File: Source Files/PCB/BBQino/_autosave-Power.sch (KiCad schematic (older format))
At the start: 14 parts, among them J1 VIN < 13V, Q1 IPD068P03L3G, U1 ADP7142ARDZ-5.0

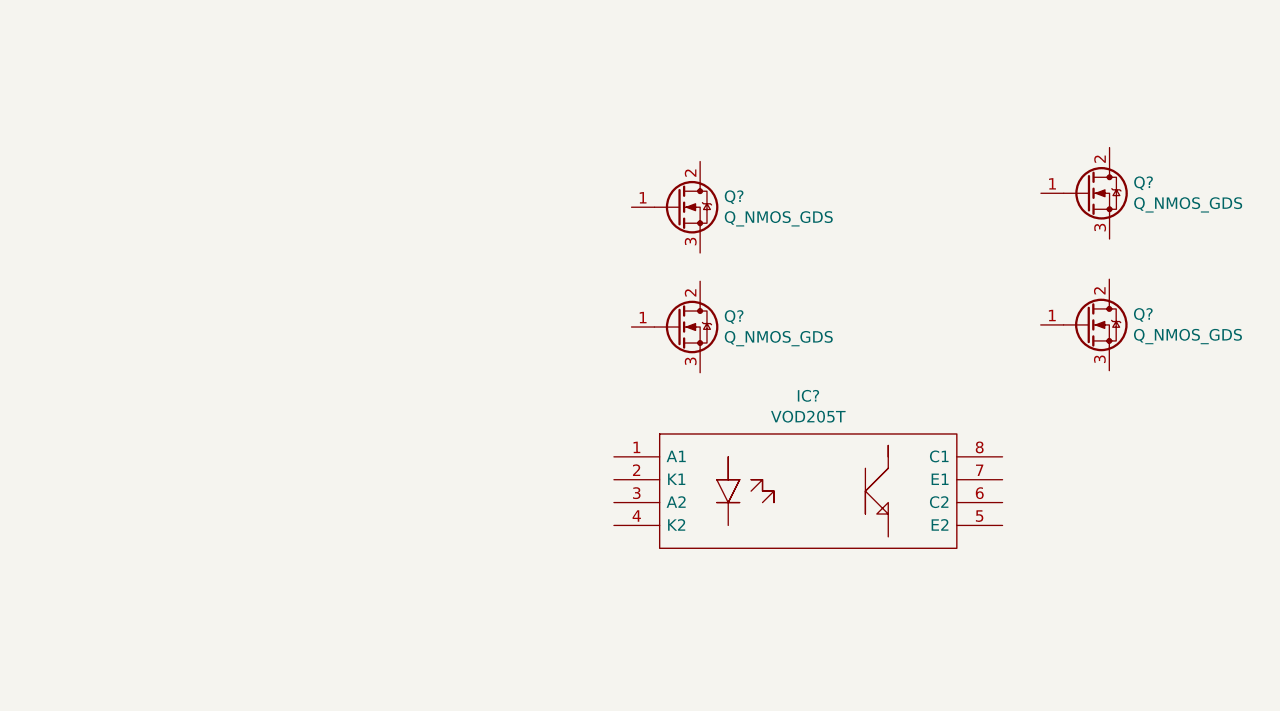
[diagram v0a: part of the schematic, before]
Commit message: added thermocouple interface
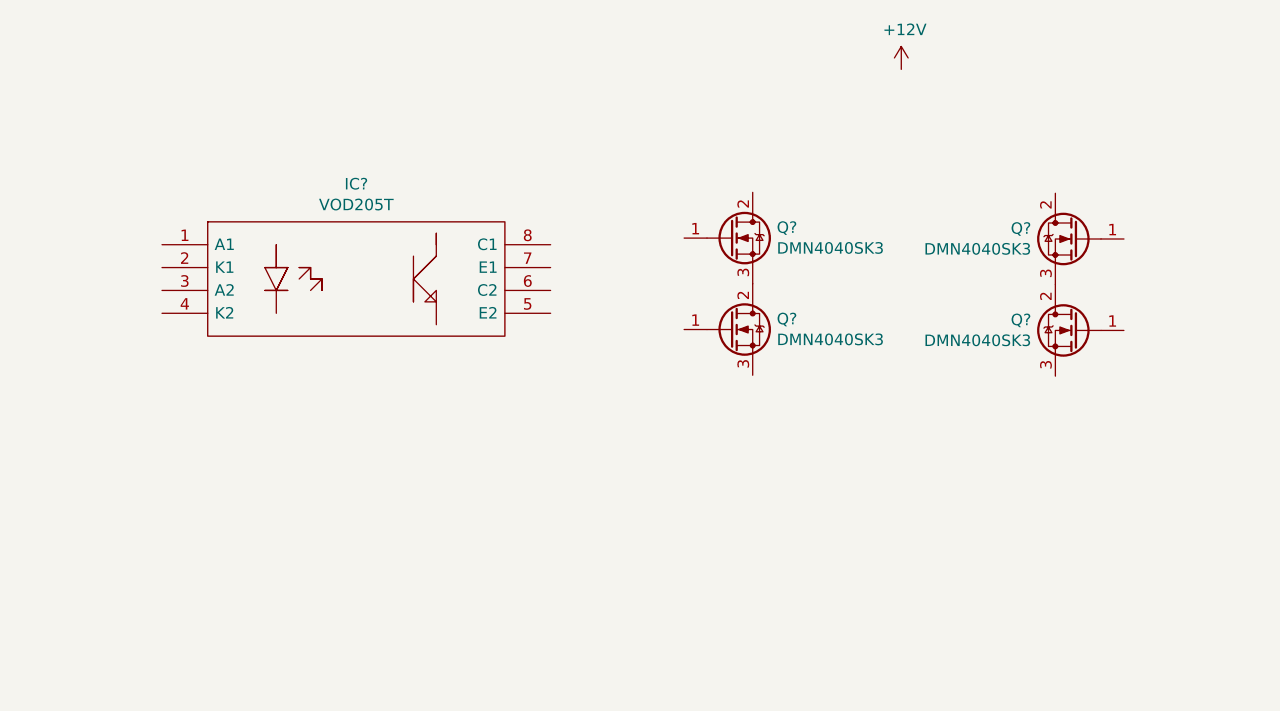
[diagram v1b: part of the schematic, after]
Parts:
- removed Q? (x3): Q_NMOS_GDS, symbol Device:Q_NMOS_GDS
- added Q? (x3): DMN4040SK3, Package_TO_SOT_SMD:TO-252-3_TabPin2, symbol Device:Q_NMOS_GDS
- Q?: value Q_NMOS_GDS -> DMN4040SK3; footprint (none) -> Package_TO_SOT_SMD:TO-252-3_TabPin2
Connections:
- net at Q?.3 (S): now also Q?.2 (D)
- new net: Q?.2 (D), Q?.3 (S)
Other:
- moved on the sheet: IC?, Q?
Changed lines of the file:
@@
 L BBQino-rescue:VOD205T IC?
 U 1 1 615B3951
-P 7605 2493
-F 0 "IC?" H 8455 2758 50  0000 C CNN
-F 1 "VOD205T" H 8455 2667 50  0000 C CNN
-F 2 "SOIC127P610X323-8N" H 9155 2593 50  0001 L CNN
-F 3 "http://www.vishay.com/docs/81956/vod205t.pdf" H 9155 2493 50  0001 L CNN
-F 4 "Vishay VOD205T DC Input, Transistor Output Dual Optocoupler, SMT SOIC 8" H 9155 2393 50  0001 L CNN "Description"
-F 5 "3.23" H 9155 2293 50  0001 L CNN "Height"
-F 6 "Vishay" H 9155 2193 50  0001 L CNN "Manufacturer_Name"
-F 7 "VOD205T" H 9155 2093 50  0001 L CNN "Manufacturer_Part_Number"
-F 8 "78-VOD205T" H 9155 1993 50  0001 L CNN "Mouser Part Number"
-F 9 "https://www.mouser.co.uk/ProductDetail/Vishay-Semiconductors/VOD205T?qs=OZzrG8p9eNh%2FWG3FDe7e4g%3D%3D" H 9155 1893 50  0001 L CNN "Mouser Price/Stock"
-F 10 "VOD205T" H 9155 1793 50  0001 L CNN "Arrow Part Number"
-F 11 "https://www.arrow.com/en/products/vod205t/vishay" H 9155 1693 50  0001 L CNN "Arrow Price/Stock"
-	1    7605 2493
+P 5628 1565
+F 0 "IC?" H 6478 1830 50  0000 C CNN
+F 1 "VOD205T" H 6478 1739 50  0000 C CNN
+F 2 "SOIC127P610X323-8N" H 7178 1665 50  0001 L CNN
+F 3 "http://www.vishay.com/docs/81956/vod205t.pdf" H 7178 1565 50  0001 L CNN
+F 4 "Vishay VOD205T DC Input, Transistor Output Dual Optocoupler, SMT SOIC 8" H 7178 1465 50  0001 L CNN "Description"
+F 5 "3.23" H 7178 1365 50  0001 L CNN "Height"
+F 6 "Vishay" H 7178 1265 50  0001 L CNN "Manufacturer_Name"
+F 7 "VOD205T" H 7178 1165 50  0001 L CNN "Manufacturer_Part_Number"
+F 8 "78-VOD205T" H 7178 1065 50  0001 L CNN "Mouser Part Number"
+F 9 "https://www.mouser.co.uk/ProductDetail/Vishay-Semiconductors/VOD205T?qs=OZzrG8p9eNh%2FWG3FDe7e4g%3D%3D" H 7178 965 50  0001 L CNN "Mouser Price/Stock"
+F 10 "VOD205T" H 7178 865 50  0001 L CNN "Arrow Part Number"
+F 11 "https://www.arrow.com/en/products/vod205t/vishay" H 7178 765 50  0001 L CNN "Arrow Price/Stock"
+	1    5628 1565
+	1    0    0    -1
+$EndComp
+$Comp
+L Device:Q_NMOS_GDS Q?
+U 1 1 615C1935
+P 8112 1936
+F 0 "Q?" H 8317 1982 50  0000 L CNN
+F 1 "DMN4040SK3" H 8317 1891 50  0000 L CNN
+F 2 "Package_TO_SOT_SMD:TO-252-3_TabPin2" H 8312 2036 50  0001 C CNN
+F 3 "https://www.mouser.it/datasheet/2/115/DIODS13197_1-2541721.pdf" H 8112 1936 50  0001 C CNN
+	1    8112 1936
+	1    0    0    -1
+$EndComp
+$Comp
+L Device:Q_NMOS_GDS Q?
+U 1 1 615C31E4
+P 9636 1540
+F 0 "Q?" H 9841 1586 50  0000 L CNN
+F 1 "DMN4040SK3" H 9841 1495 50  0000 L CNN
+F 2 "Package_TO_SOT_SMD:TO-252-3_TabPin2" H 9836 1640 50  0001 C CNN
+F 3 "https://www.mouser.it/datasheet/2/115/DIODS13197_1-2541721.pdf" H 9636 1540 50  0001 C CNN
+	1    9636 1540
+	-1   0    0    -1
+$EndComp
+$Comp
+L Device:Q_NMOS_GDS Q?
+U 1 1 615C7565
+P 9636 1940
+F 0 "Q?" H 9841 1986 50  0000 L CNN
+F 1 "DMN4040SK3" H 9841 1895 50  0000 L CNN
+F 2 "Package_TO_SOT_SMD:TO-252-3_TabPin2" H 9836 2040 50  0001 C CNN
+F 3 "https://www.mouser.it/datasheet/2/115/DIODS13197_1-2541721.pdf" H 9636 1940 50  0001 C CNN
+	1    9636 1940
+	-1   0    0    -1
+$EndComp
+$Comp
+L power:+12V #PWR?
+U 1 1 615FE2CF
+P 8862 798
+F 0 "#PWR?" H 8862 648 50  0001 C CNN
+F 1 "+12V" H 8877 971 50  0000 C CNN
+F 2 "" H 8862 798 50  0001 C CNN
+F 3 "" H 8862 798 50  0001 C CNN
+	1    8862 798
 	1    0    0    -1
 $EndComp
@@
 L Device:Q_NMOS_GDS Q?
 U 1 1 615B46B7
-P 9673 1340
-F 0 "Q?" H 9877 1386 50  0000 L CNN
-F 1 "Q_NMOS_GDS" H 9877 1295 50  0000 L CNN
-F 2 "" H 9873 1440 50  0001 C CNN
-F 3 "~" H 9673 1340 50  0001 C CNN
-	1    9673 1340
+P 8112 1536
+F 0 "Q?" H 8317 1582 50  0000 L CNN
+F 1 "DMN4040SK3" H 8317 1491 50  0000 L CNN
+F 2 "Package_TO_SOT_SMD:TO-252-3_TabPin2" H 8312 1636 50  0001 C CNN
+F 3 "https://www.mouser.it/datasheet/2/115/DIODS13197_1-2541721.pdf" H 8112 1536 50  0001 C CNN
+	1    8112 1536
 	1    0    0    -1
 $EndComp
-$Comp
-L Device:Q_NMOS_GDS Q?
-U 1 1 615B8A4A
-P 9672 1916
-F 0 "Q?" H 9876 1962 50  0000 L CNN
-F 1 "Q_NMOS_GDS" H 9876 1871 50  0000 L CNN
-F 2 "" H 9872 2016 50  0001 C CNN
-F 3 "~" H 9672 1916 50  0001 C CNN
-	1    9672 1916
-	1    0    0    -1
-$EndComp
-$Comp
-L Device:Q_NMOS_GDS Q?
-U 1 1 615B90C8
-P 7882 1401
-F 0 "Q?" H 8086 1447 50  0000 L CNN
-F 1 "Q_NMOS_GDS" H 8086 1356 50  0000 L CNN
-F 2 "" H 8082 1501 50  0001 C CNN
-F 3 "~" H 7882 1401 50  0001 C CNN
-	1    7882 1401
-	1    0    0    -1
-$EndComp
-$Comp
-L Device:Q_NMOS_GDS Q?
-U 1 1 615B995D
-P 7882 1925
-F 0 "Q?" H 8086 1971 50  0000 L CNN
-F 1 "Q_NMOS_GDS" H 8086 1880 50  0000 L CNN
-F 2 "" H 8082 2025 50  0001 C CNN
-F 3 "~" H 7882 1925 50  0001 C CNN
-	1    7882 1925
-	1    0    0    -1
-$EndComp
